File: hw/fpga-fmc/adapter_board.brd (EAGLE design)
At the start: 68.9 x 85.5 mm, 176 parts, among them IC1 M24C02, J1 5569262-1, J2 ASP-134488-01, U1 ADM3066E, U10 ADM3066E, U11 ADM3066E, U12 ADM3066E, U13 ADM3066E, U14 ADM3066E, U15 ADM3066E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

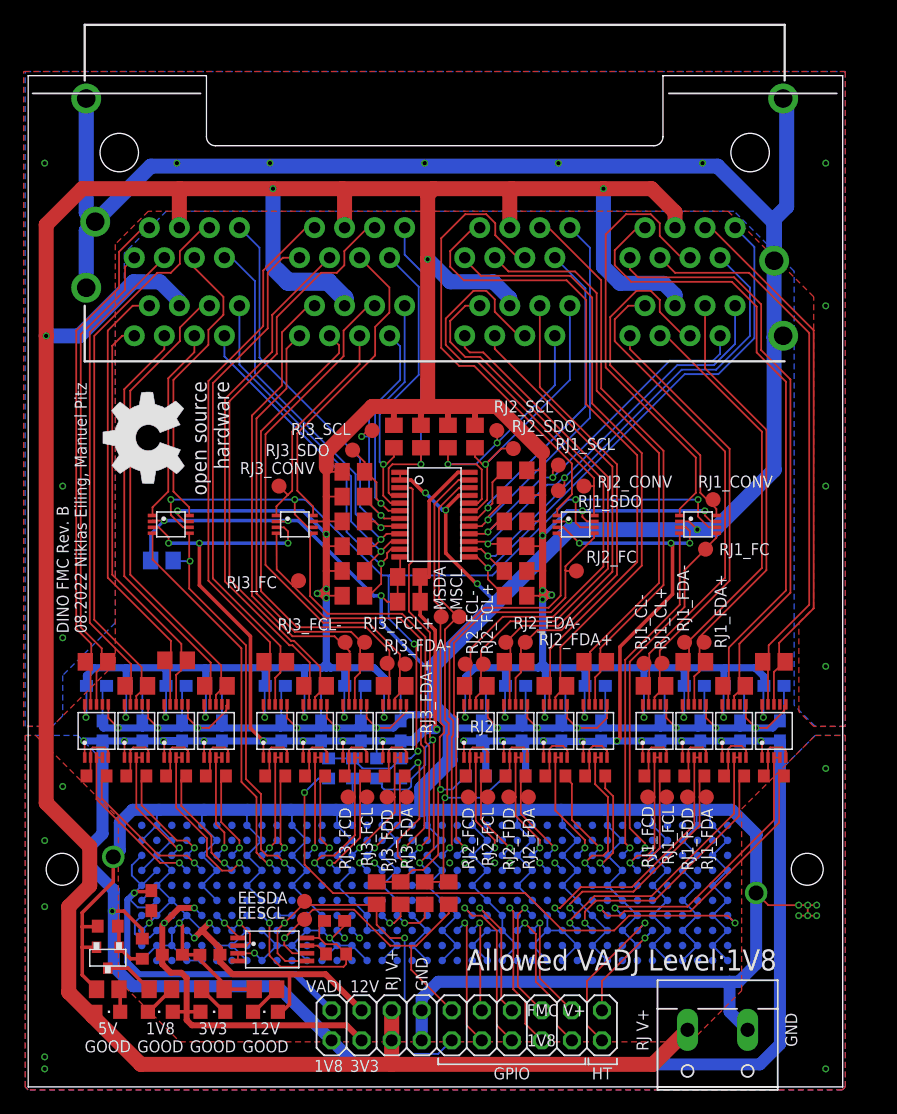
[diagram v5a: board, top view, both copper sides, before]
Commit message: hw/fpga-fmc: fix wrong connection on bottom row rj-45 connectors
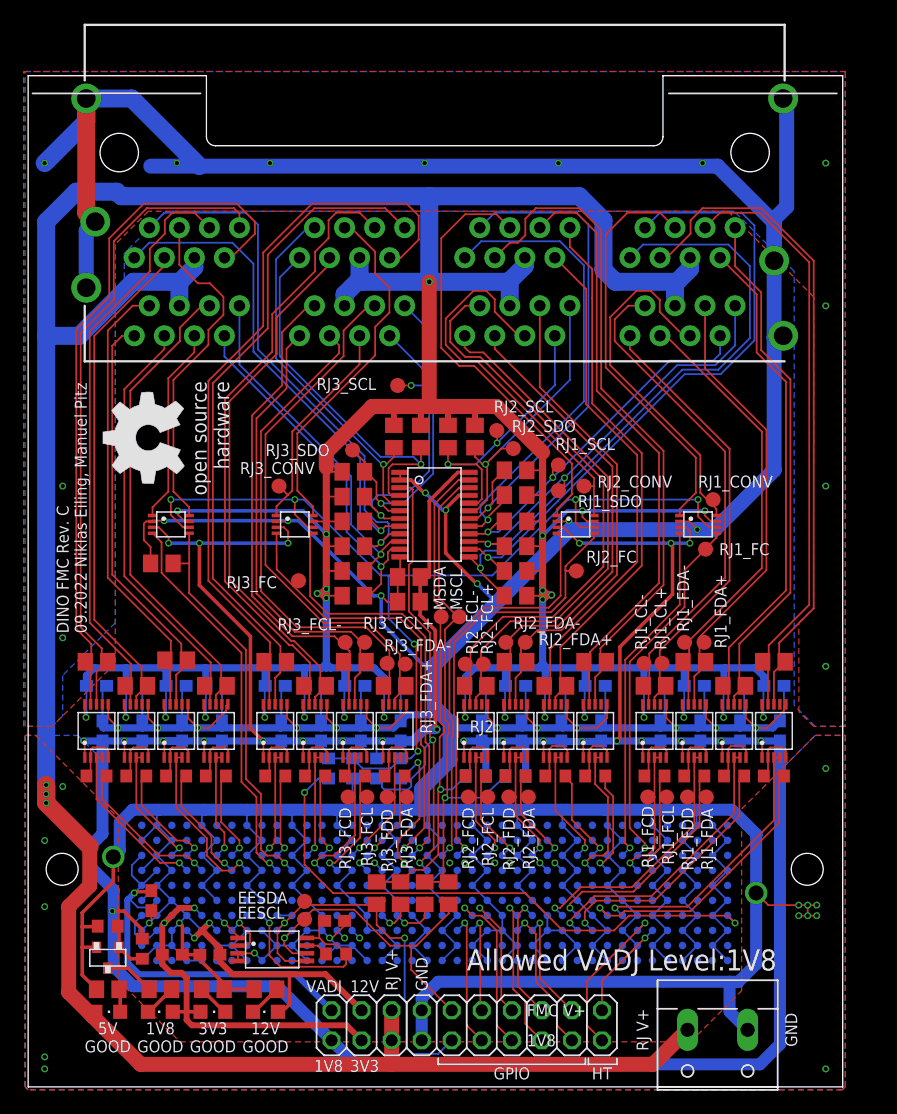
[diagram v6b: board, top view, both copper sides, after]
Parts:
- moved RJ3_SCL 4.38 mm to (31.4, 59.3)
- moved R59 0.25 mm to (11.4, 44.3), flipped to the top, turned to 180 degrees
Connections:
- net 5V: now also J1.5.5, J1.6.5, J1.7.5, J1.8.5; no longer J1.5.4, J1.6.4, J1.7.4, J1.8.4
- net RJ5_CLK_N: now also J1.5.7; no longer J1.5.2
- net RJ5_CLK_P: now also J1.5.8; no longer J1.5.1
- net RJ5_CONV: now also J1.5.4; no longer J1.5.5
- net RJ5_DATA_N: now also J1.5.6; no longer J1.5.3
- net RJ5_DATA_P: now also J1.5.3; no longer J1.5.6
- net RJ5_SCL: now also J1.5.2; no longer J1.5.7
- net RJ5_SDO: now also J1.5.1; no longer J1.5.8
- net RJ6_CLK_N: now also J1.6.7; no longer J1.6.2
- net RJ6_CLK_P: now also J1.6.8; no longer J1.6.1
- net RJ6_CONV: now also J1.6.4; no longer J1.6.5
- net RJ6_DATA_N: now also J1.6.6; no longer J1.6.3
- net RJ6_DATA_P: now also J1.6.3; no longer J1.6.6
- net RJ6_SCL: now also J1.6.2; no longer J1.6.7
- net RJ6_SDO: now also J1.6.1; no longer J1.6.8
- net RJ7_CLK_N: now also J1.7.7; no longer J1.7.2
- net RJ7_CLK_P: now also J1.7.8; no longer J1.7.1
- net RJ7_CONV: now also J1.7.4; no longer J1.7.5
- net RJ7_DATA_N: now also J1.7.6; no longer J1.7.3
- net RJ7_DATA_P: now also J1.7.3; no longer J1.7.6
- net RJ7_SCL: now also J1.7.2; no longer J1.7.7
- net RJ7_SDO: now also J1.7.1; no longer J1.7.8
- net RJ8_CLK_N: now also J1.8.7; no longer J1.8.2
- net RJ8_CLK_P: now also J1.8.8; no longer J1.8.1
- net RJ8_CONV: now also J1.8.4; no longer J1.8.5
- net RJ8_DATA_N: now also J1.8.6; no longer J1.8.3
- net RJ8_DATA_P: now also J1.8.3; no longer J1.8.6
- net RJ8_SCL: now also J1.8.2; no longer J1.8.7
- net RJ8_SDO: now also J1.8.1; no longer J1.8.8
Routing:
- net RJ7_CLK_N: track 47.0 -> 63.1 mm
- net RJ8_CLK_N: track 44.1 -> 60.1 mm
- net RJ8_CLK_P: track 41.0 -> 54.8 mm
- net 5V: track 525.5 -> 511.8 mm, vias 31 -> 32
- net 0V: track 808.3 -> 821.1 mm
- net RJ8_SCL: track 33.1 -> 45.8 mm
- net RJ5_CLK_N: track 55.2 -> 42.5 mm
- net RJ6_CLK_N: track 56.8 -> 44.1 mm
- net RJ5_SCL: track 41.3 -> 53.8 mm
- net RJ7_CLK_P: track 44.6 -> 56.8 mm
- net RJ6_SCL: track 31.4 -> 43.3 mm
- net RJ5_DATA_P: track 46.2 -> 56.6 mm
- net RJ6_DATA_P: track 47.9 -> 57.4 mm
- net RJ8_SDO: track 33.6 -> 42.0 mm
- net RJ5_SDO: track 45.5 -> 53.5 mm
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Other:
- board text added: "DINO FMC Rev. C 09.2022 Niklas Eiling, Manuel Pitz"
- board text removed: "DINO FMC Rev. B 08.2022 Niklas Eiling, Manuel Pitz"

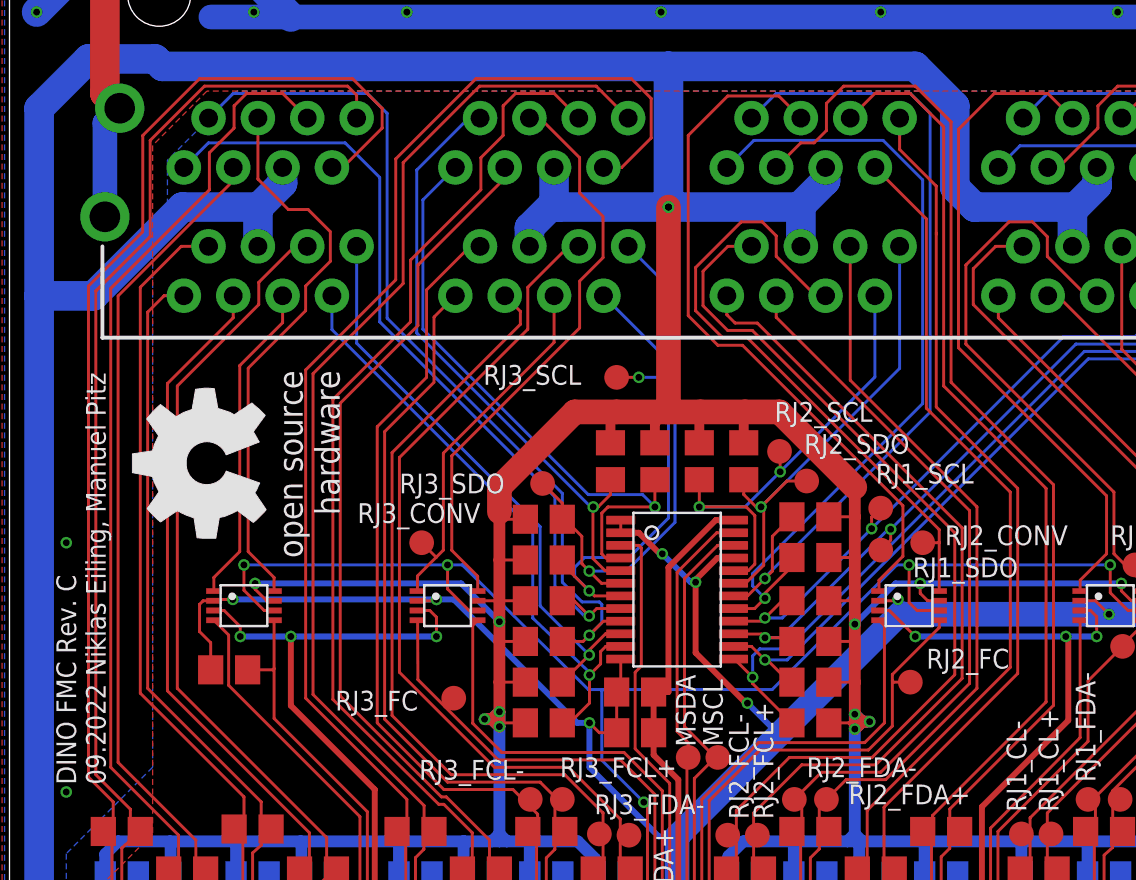
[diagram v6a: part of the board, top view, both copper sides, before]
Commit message: hw/fpga-fmc: fix more issues on adapter board
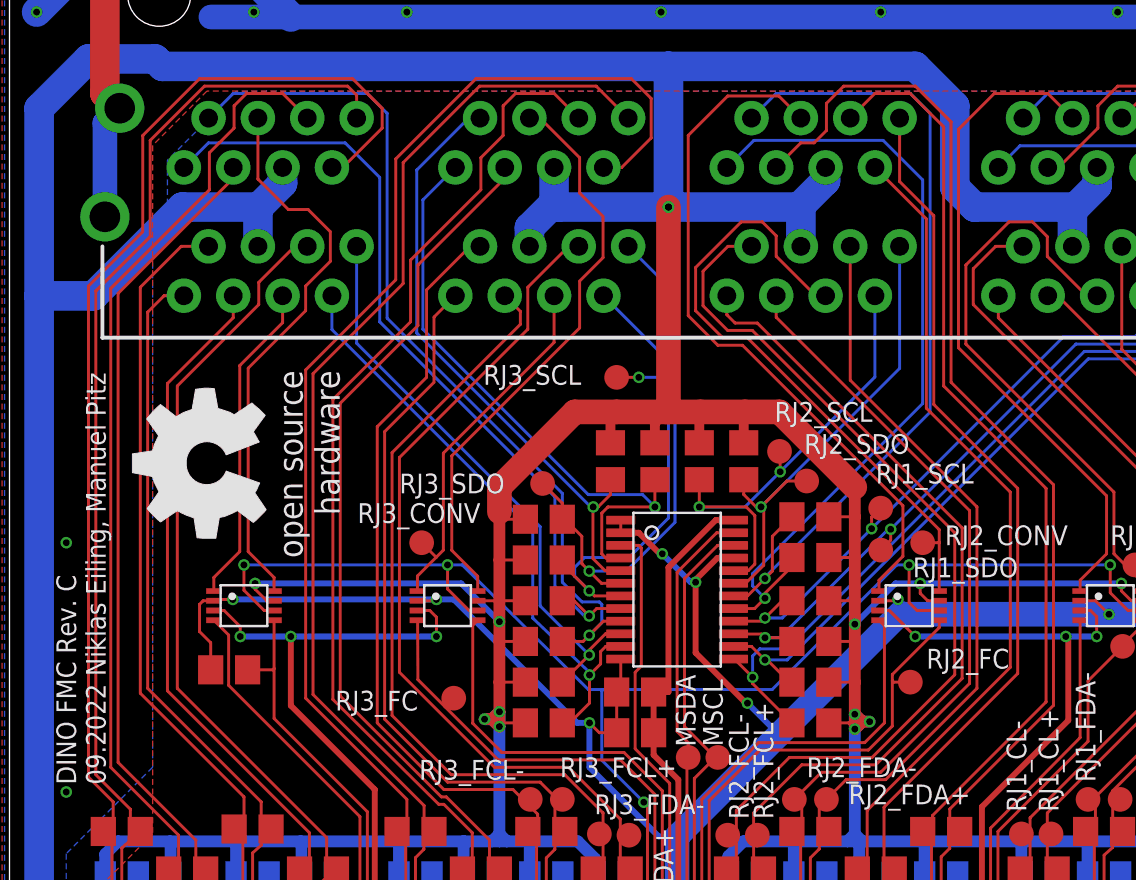
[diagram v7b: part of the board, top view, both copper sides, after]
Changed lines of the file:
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@@
 <wire x1="10.0925" y1="47.8115" x2="10.642" y2="47.8115" width="0.1524" layer="1"/>
 <wire x1="9.906" y1="47.625" x2="10.0925" y2="47.8115" width="0.1524" layer="1"/>
-<wire x1="63.964" y1="83.572" x2="67.564" y2="78.105" width="0" layer="19" extent="1-1"/>
-<wire x1="35.135" y1="10.685" x2="33.865" y2="10.685" width="0" layer="19" extent="16-16"/>
-<wire x1="12.7" y1="78.105" x2="10.491" y2="77.851" width="0" layer="19" extent="16-16"/>
-<wire x1="67.564" y1="35.56" x2="64.0325" y2="33.909" width="0" layer="19" extent="16-16"/>
-<wire x1="67.564" y1="66.04" x2="63.964" y2="63.51" width="0" layer="19" extent="1-1"/>
-<wire x1="1.524" y1="15.24" x2="6.008" y2="13.589" width="0" layer="19" extent="1-1"/>
-<wire x1="3.048" y1="37.973" x2="6.7555" y2="33.909" width="0" layer="19" extent="16-16"/>
-<wire x1="67.564" y1="26.924" x2="63.6905" y2="30.949" width="0" layer="19" extent="16-16"/>
-<wire x1="1.524" y1="20.828" x2="1.524" y2="15.24" width="0" layer="19" extent="1-1"/>
-<wire x1="3.048" y1="25.4" x2="1.524" y2="20.828" width="0" layer="19" extent="1-1"/>
-<wire x1="1.524" y1="2.54" x2="5.908" y2="8.255" width="0" layer="19" extent="1-1"/>
-<wire x1="1.524" y1="1.524" x2="1.524" y2="2.54" width="0" layer="19" extent="1-1"/>
-<wire x1="67.564" y1="1.524" x2="60.96" y2="4.826" width="0" layer="19" extent="1-1"/>
-<wire x1="20.574" y1="78.105" x2="12.7" y2="78.105" width="0" layer="19" extent="1-1"/>
-<wire x1="3.048" y1="50.8" x2="10.642" y2="47.8115" width="0" layer="19" extent="1-1"/>
-<wire x1="57.15" y1="78.105" x2="63.964" y2="83.572" width="0" layer="19" extent="1-1"/>
-<wire x1="67.564" y1="50.8" x2="56.7055" y2="47.117" width="0" layer="19" extent="1-1"/>
-<wire x1="44.958" y1="78.105" x2="57.15" y2="78.105" width="0" layer="19" extent="1-1"/>
-<wire x1="33.655" y1="78.105" x2="44.958" y2="78.105" width="0" layer="19" extent="1-1"/>
 </signal>
 <signal name="RJ5_SDO">
@@
 <wire x1="45.12723125" y1="33.432021875" x2="45.50823125" y2="33.857846875" width="0.1524" layer="1"/>
 <wire x1="45.50823125" y1="33.857846875" x2="45.654" y2="33.909" width="0.1524" layer="1"/>
-<wire x1="47.8155" y1="66.7385" x2="47.8155" y2="66.675" width="0.1524" layer="1"/>
-<wire x1="47.8155" y1="66.675" x2="47.8155" y2="57.785" width="0.1524" layer="1"/>
-<wire x1="47.8155" y1="57.785" x2="52.0065" y2="53.594" width="0.1524" layer="1"/>
+<wire x1="47.6885" y1="67.6275" x2="47.6885" y2="57.912" width="0.1524" layer="1"/>
+<wire x1="47.6885" y1="57.912" x2="52.0065" y2="53.594" width="0.1524" layer="1"/>
 <wire x1="52.0065" y1="53.594" x2="52.0065" y2="44.069" width="0.1524" layer="1"/>
 <wire x1="44.704" y1="32.349" x2="44.704" y2="32.959" width="0.1524" layer="1"/>
 <wire x1="45.12723125" y1="37.18973125" x2="45.12723125" y2="33.432021875" width="0.1524" layer="1"/>
 <wire x1="52.0065" y1="44.069" x2="45.12723125" y2="37.18973125" width="0.1524" layer="1"/>
-<wire x1="47.8155" y1="66.7385" x2="47.8155" y2="69.1515" width="0.1524" layer="1"/>
-<wire x1="45.93" y1="71.037" x2="45.93" y2="72.65" width="0.1524" layer="1"/>
-<wire x1="47.8155" y1="69.1515" x2="45.93" y2="71.037" width="0.1524" layer="1"/>
+<wire x1="45.93" y1="69.386" x2="45.93" y2="72.65" width="0.1524" layer="1"/>
+<wire x1="47.6885" y1="67.6275" x2="45.93" y2="69.386" width="0.1524" layer="1"/>
 </signal>
 <signal name="RJ2_SDO">
@@
 <contactref element="U2" pad="P7"/>
 <contactref element="R22" pad="1"/>
-<wire x1="5.715" y1="63.5" x2="5.715" y2="39.497" width="0.1524" layer="1"/>
+<wire x1="5.715" y1="63.627" x2="5.715" y2="39.497" width="0.1524" layer="1"/>
 <wire x1="9.271" y1="32.349" x2="9.271" y2="33.059" width="0.1524" layer="1"/>
 <wire x1="9.271" y1="33.059" x2="10.221" y2="33.909" width="0.1524" layer="1"/>
@@
 <wire x1="9.7155" y1="34.3145" x2="9.7155" y2="35.4965" width="0.1524" layer="1"/>
 <wire x1="9.7155" y1="35.4965" x2="5.715" y2="39.497" width="0.1524" layer="1"/>
-<wire x1="5.715" y1="63.5" x2="11.049" y2="68.834" width="0.15" layer="1"/>
-<wire x1="11.049" y1="68.834" x2="11.64" y2="69.425" width="0.1524" layer="1"/>
-<wire x1="11.64" y1="69.425" x2="11.64" y2="70.11" width="0.1524" layer="1"/>
+<wire x1="5.715" y1="63.627" x2="11.64" y2="69.552" width="0.1524" layer="1"/>
+<wire x1="11.64" y1="69.552" x2="11.64" y2="70.11" width="0.1524" layer="1"/>
 </signal>
 <signal name="RJ8_CONV">
